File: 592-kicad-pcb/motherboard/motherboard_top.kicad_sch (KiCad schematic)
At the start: 27 parts, among them J17 Conn_02x01, J18 Conn_02x01, J21 Conn_02x01, J22 Conn_02x01, J25 Conn_02x01, J26 Conn_02x01, U14 74CBTLV3257PW,118, U15 74CBTLV3257PW,118, U17 74CBTLV3257PW,118, U18 SN74LVC1G00DCK, U19 SN74LVC1G14DBV, U20 74CBTLV3257PW,118, U21 SN74LVC1G14DBV

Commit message: john's notes
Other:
- sheet pmic_on_boarding ports: added 5V0_EXTERNAL, 5V0_NUCLEO, 5V0_ON_BOARD, GND; removed none
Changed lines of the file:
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@@
 		(exclude_from_sim no)
 		(at 156.21 238.76 0)
-		(size 62.23 29.21)
+		(size 62.23 124.46)
 		(margins 0.9525 0.9525 0.9525 0.9525)
 		(stroke
@@
 	)
 	(sheet
-		(at 342.9 203.2)
+		(at 163.83 344.17)
 		(size 44.45 40.64)
 		(exclude_from_sim no)
@@
 		)
 		(property "Sheetname" "pmic_switching"
-			(at 342.9 202.4884 0)
+			(at 163.83 343.4584 0)
 			(effects
 				(font
@@
 		)
 		(property "Sheetfile" "pmic_switching.kicad_sch"
-			(at 342.9 244.4246 0)
+			(at 163.83 385.3946 0)
 			(effects
 				(font
@@
 	)
 	(sheet
-		(at 290.83 203.2)
+		(at 165.1 297.18)
 		(size 41.91 40.64)
 		(exclude_from_sim no)
@@
 		)
 		(property "Sheetname" "pmic_supplies"
-			(at 290.83 202.4884 0)
+			(at 165.1 296.4684 0)
 			(effects
 				(font
@@
 		)
 		(property "Sheetfile" "pmic_supplies.kicad_sch"
-			(at 290.83 244.4246 0)
+			(at 165.1 338.4046 0)
 			(effects
 				(font
@@
 	)
 	(sheet
-		(at 233.68 203.2)
+		(at 165.1 250.19)
 		(size 41.91 40.64)
 		(exclude_from_sim no)
@@
 		)
 		(property "Sheetname" "pmic_on_boarding"
-			(at 233.68 202.4884 0)
+			(at 165.1 249.4784 0)
 			(effects
 				(font
@@
 		)
 		(property "Sheetfile" "pmic_on_boarding.kicad_sch"
-			(at 233.68 244.4246 0)
+			(at 165.1 291.4146 0)
 			(effects
 				(font
@@
 			)
 		)
+		(pin "5V0_ON_BOARD" output
+			(at 165.1 259.08 180)
+			(effects
+				(font
+					(size 1.27 1.27)
+				)
+				(justify left)
+			)
+		)
+		(pin "5V0_NUCLEO" input
+			(at 165.1 264.16 180)
+			(effects
+				(font
+					(size 1.27 1.27)
+				)
+				(justify left)
+			)
+		)
+		(pin "GND" bidirectional
+			(at 185.42 290.83 270)
+			(effects
+				(font
+					(size 1.27 1.27)
+				)
+				(justify left)
+			)
+		)
+		(pin "5V0_EXTERNAL" input
+			(at 207.01 261.62 0)
+			(effects
+				(font
+					(size 1.27 1.27)
+				)
+				(justify right)
+			)
+		)

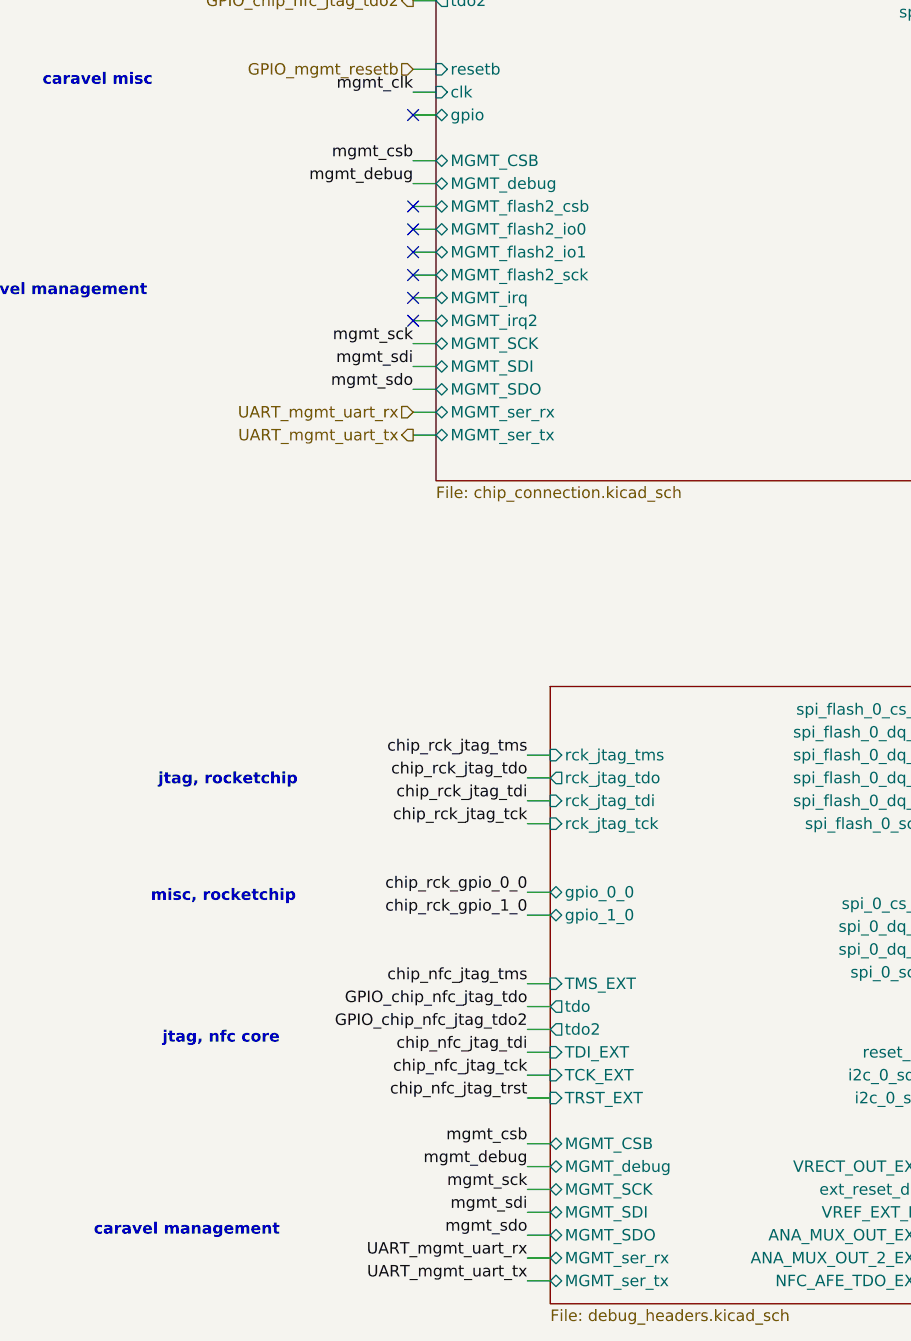
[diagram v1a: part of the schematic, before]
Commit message: map to STM pins
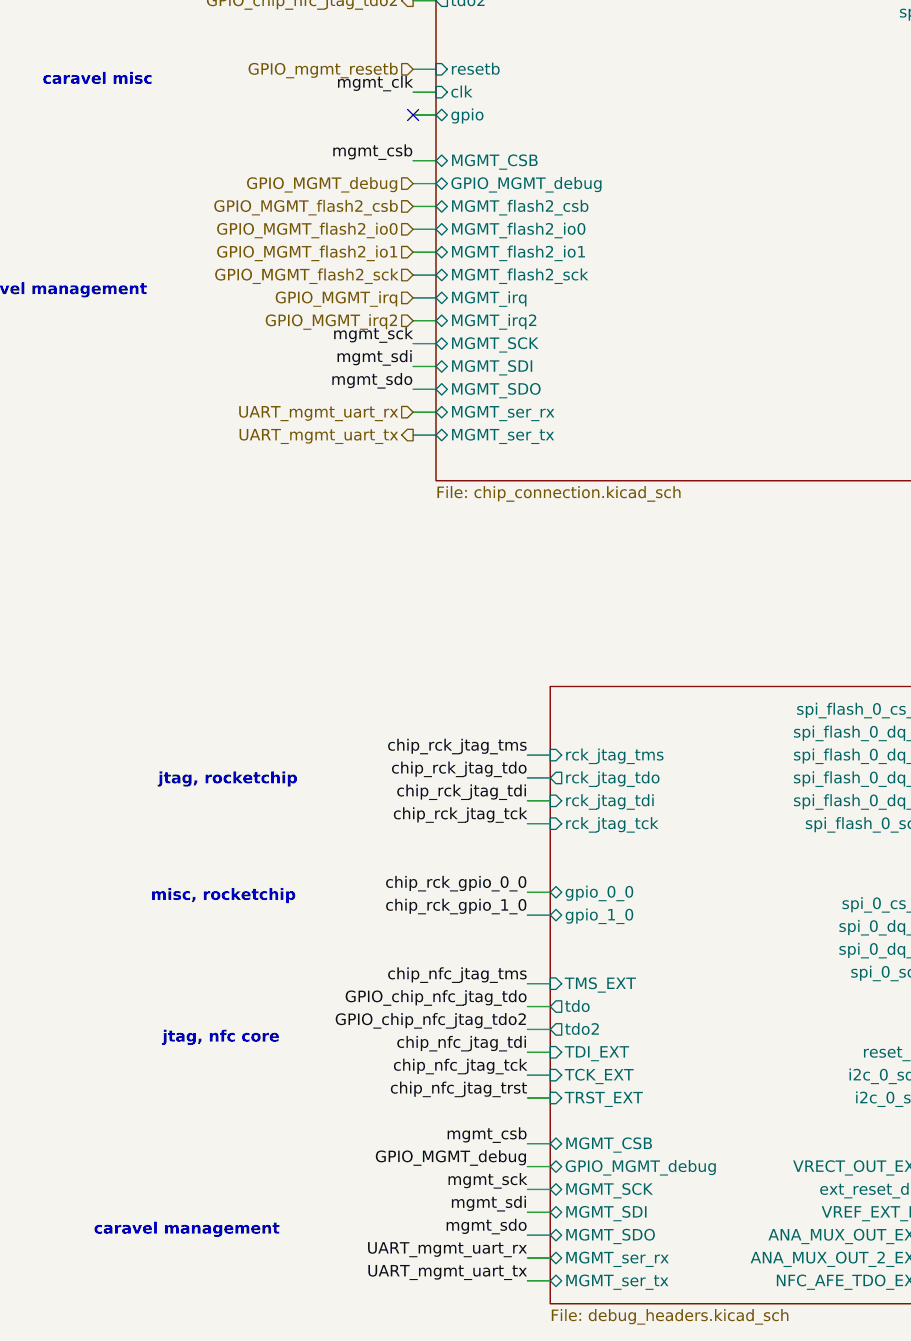
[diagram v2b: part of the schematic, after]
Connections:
- no-connect marks 14 -> 8
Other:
- sheet chip_connection ports: added GPIO_MGMT_debug; removed MGMT_debug
- sheet debug_headers ports: added GPIO_MGMT_debug; removed MGMT_debug
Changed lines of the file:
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@@
 	)
 	(no_connect
-		(at 80.01 115.57)
-	)
-	(no_connect
-		(at 80.01 105.41)
-	)
-	(no_connect
-		(at 80.01 113.03)
-	)
-	(no_connect
 		(at 166.37 246.38)
 	)
@@
 	)
 	(no_connect
-		(at 80.01 107.95)
-	)
-	(no_connect
-		(at 80.01 110.49)
-	)
-	(no_connect
 		(at 405.13 152.4)
 	)
@@
 	)
 	(no_connect
-		(at 80.01 102.87)
-	)
-	(no_connect
 		(at 389.89 149.86)
 	)
@@
 		)
 	)
-	(label "mgmt_debug"
+	(label "GPIO_MGMT_debug"
 		(at 92.71 209.55 180)
 		(effects
@@
 		)
 	)
-	(label "mgmt_debug"
-		(at 80.01 100.33 180)
-		(effects
-			(font
-				(size 1.27 1.27)
-			)
-			(justify right bottom)
-		)
-	)
 	(label "rck_mem_source_enB"
 		(at 364.49 66.04 270)
@@
 		)
 	)
+	(hierarchical_label "GPIO_MGMT_debug"
+		(shape input)
+		(at 80.01 100.33 180)
+		(effects
+			(font
+				(size 1.27 1.27)
+			)
+			(justify right)
+		)
+	)
 	(hierarchical_label "GPIO_ftdi_jtag_src_en"
 		(shape input)
@@
 		)
 	)
+	(hierarchical_label "GPIO_MGMT_flash2_io1"
+		(shape input)
+		(at 80.01 107.95 180)
+		(effects
+			(font
+				(size 1.27 1.27)
+			)
+			(justify right)
+		)
+	)
+	(hierarchical_label "GPIO_MGMT_flash2_csb"
+		(shape input)
+		(at 80.01 102.87 180)
+		(effects
+			(font
+				(size 1.27 1.27)
+			)
+			(justify right)
+		)
+	)
+	(hierarchical_label "GPIO_MGMT_flash2_io0"
+		(shape input)
+		(at 80.01 105.41 180)
+		(effects
+			(font
+				(size 1.27 1.27)
+			)
+			(justify right)
+		)
+	)
+	(hierarchical_label "GPIO_MGMT_flash2_sck"
+		(shape input)
+		(at 80.01 110.49 180)
+		(effects
+			(font
+				(size 1.27 1.27)
+			)
+			(justify right)
+		)
+	)
+	(hierarchical_label "GPIO_MGMT_irq"
+		(shape input)
+		(at 80.01 113.03 180)
+		(effects
+			(font
+				(size 1.27 1.27)
+			)
+			(justify right)
+		)
+	)
+	(hierarchical_label "GPIO_MGMT_irq2"
+		(shape input)
+		(at 80.01 115.57 180)
+		(effects
+			(font
+				(size 1.27 1.27)
+			)
+			(justify right)
+		)
+	)
 	(hierarchical_label "GPIO_rck_mem_sel_sdB"
 		(shape input)
@@
 			)
 		)
-		(pin "MGMT_debug" bidirectional
+		(pin "GPIO_MGMT_debug" bidirectional
 			(at 95.25 209.55 180)
 			(effects
@@
 			)
 		)
-		(pin "MGMT_debug" bidirectional
+		(pin "GPIO_MGMT_debug" bidirectional
 			(at 82.55 100.33 180)
 			(effects

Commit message: updates to routing
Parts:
- renumbered C38 to C37, C41 to C38, C34 to C39, C35 to C41, J26 to J23, J17 to J24, J18 to J26, R56 to R52, R57 to R53, R49 to R54, R48 to R55, R50 to R56, R52 to R57, R53 to R58, U19 to U15, U18 to U16, U14 to U17, U21 to U18, U17 to U19, U15 to U20, U20 to U21
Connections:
- net GPIO_chip_nfc_jtag_tdo: now also U19.3; no longer U19.10
- net chip_nfc_jtag_tms: now also U19.10; no longer U19.3
- net chip_rck_jtag_tdo: now also U19.2; no longer U19.11
- net chip_rck_jtag_tms: now also U19.11; no longer U19.2
- net ftdi1_jtag_tdo: now also U19.4; no longer U19.9
- net ftdi1_jtag_tms: now also U19.9; no longer U19.4

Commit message: finalize termination
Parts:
- added C53: 10n, symbol Device:C_Small
- added R10, R14, R15, R16, R19, R71, R72, R8, R9, R98, R99: 10k, Resistor_SMD:R_0402_1005Metric, symbol Device:R_Small
- added R104, R17: 1M, Resistor_SMD:R_0402_1005Metric, symbol Device:R_Small
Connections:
- net +3V3: now also R10.1, R14.1, R15.1, R16.1, R71.1, R72.1, R8.1, R9.1, R98.1, R99.1
- net GND: now also C53.2, R104.2, R17.2, R19.2
- net chip_nfc_jtag_tck: now also R17.1
- net chip_nfc_jtag_tdi: now also R14.2
- net chip_nfc_jtag_tms: now also R16.2, R9.2
- net chip_nfc_jtag_trst: now also C53.1, R19.1
- net chip_rck_jtag_tck: now also R104.1
- net chip_rck_jtag_tdi: now also R10.2
- net chip_rck_jtag_tms: now also R15.2, R8.2
- net ftdi_spi_cs: now also R71.2
- net ftdi_spi_sck: now also R72.2
- net rck_mem_cs: now also R98.2
- net rck_mem_sck: now also R99.2
- net GPIO_SPI_MGMT_enable renamed GPIO_MGMT_enable
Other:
- sheet chip_connection ports: added GPIO_MGMT_enable; removed none
- note added: "SPI pull-ups to ensure OK state w/out daughter"
- note added: "also allow disabling for off-chip mem"

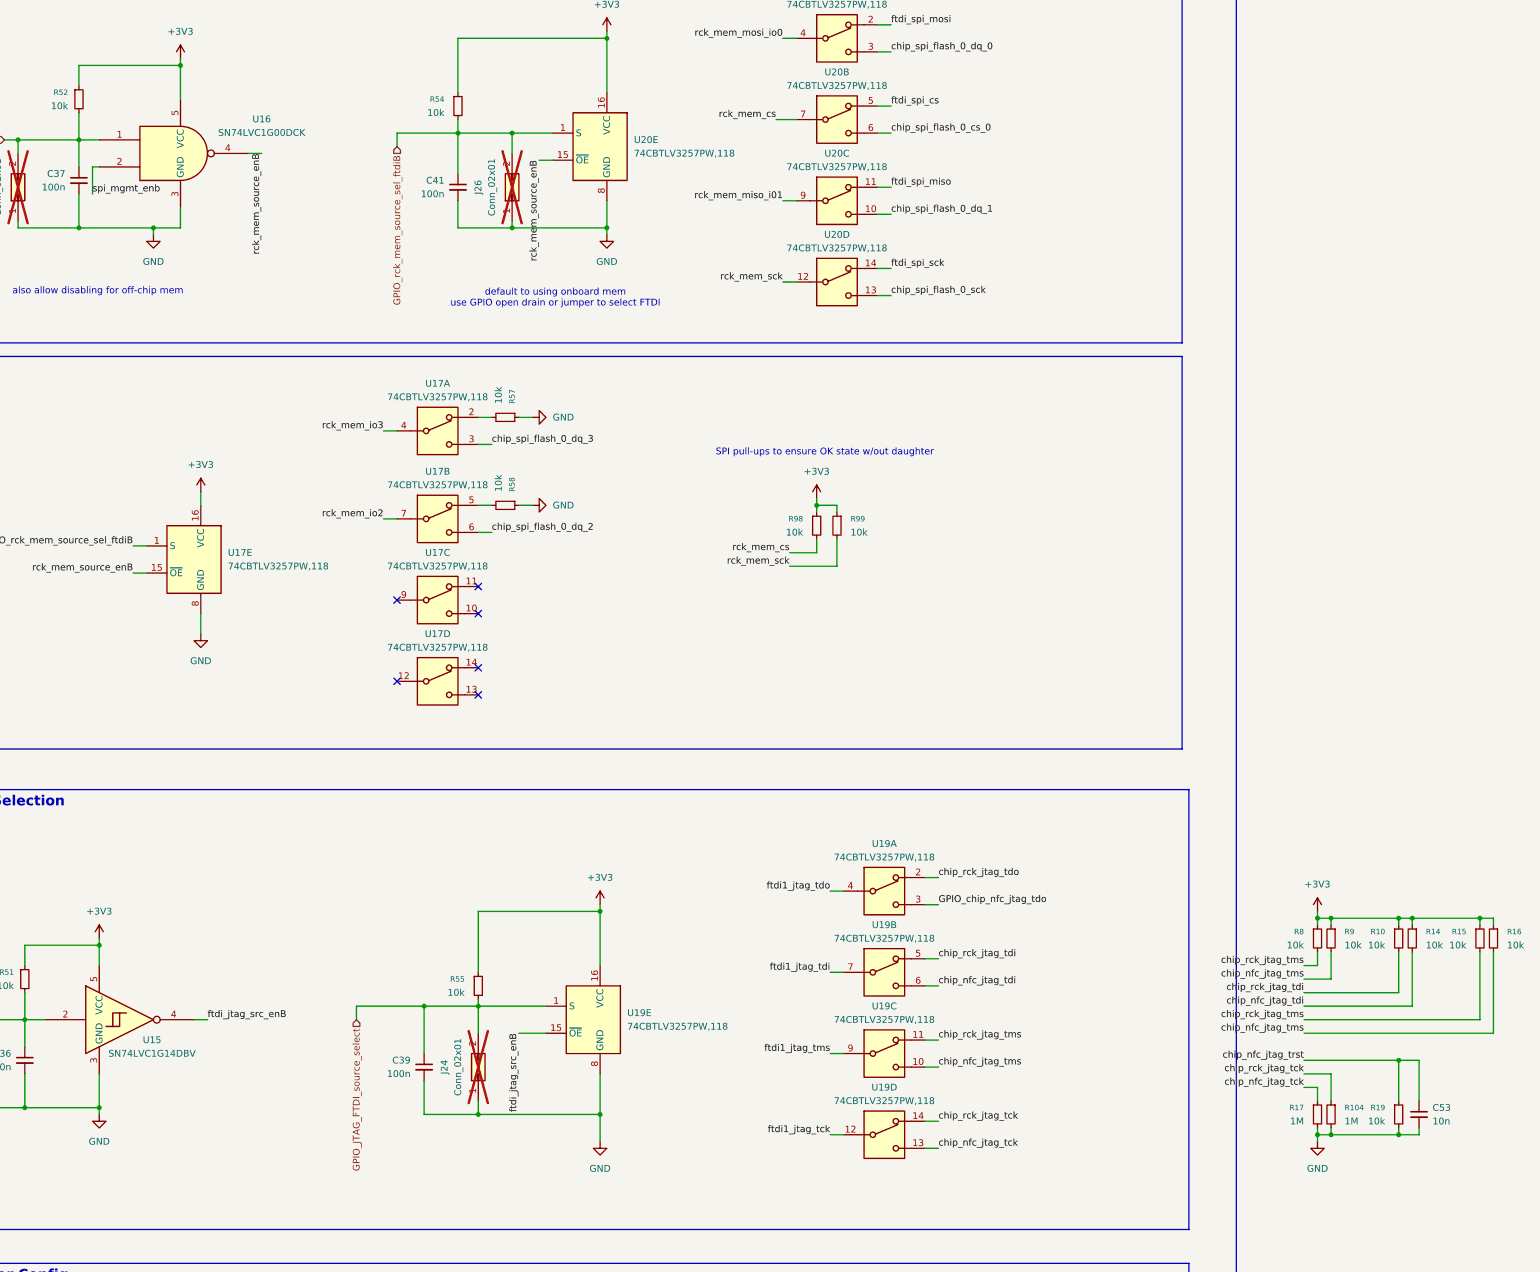
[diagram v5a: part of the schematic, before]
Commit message: update jlcpcb part numbers
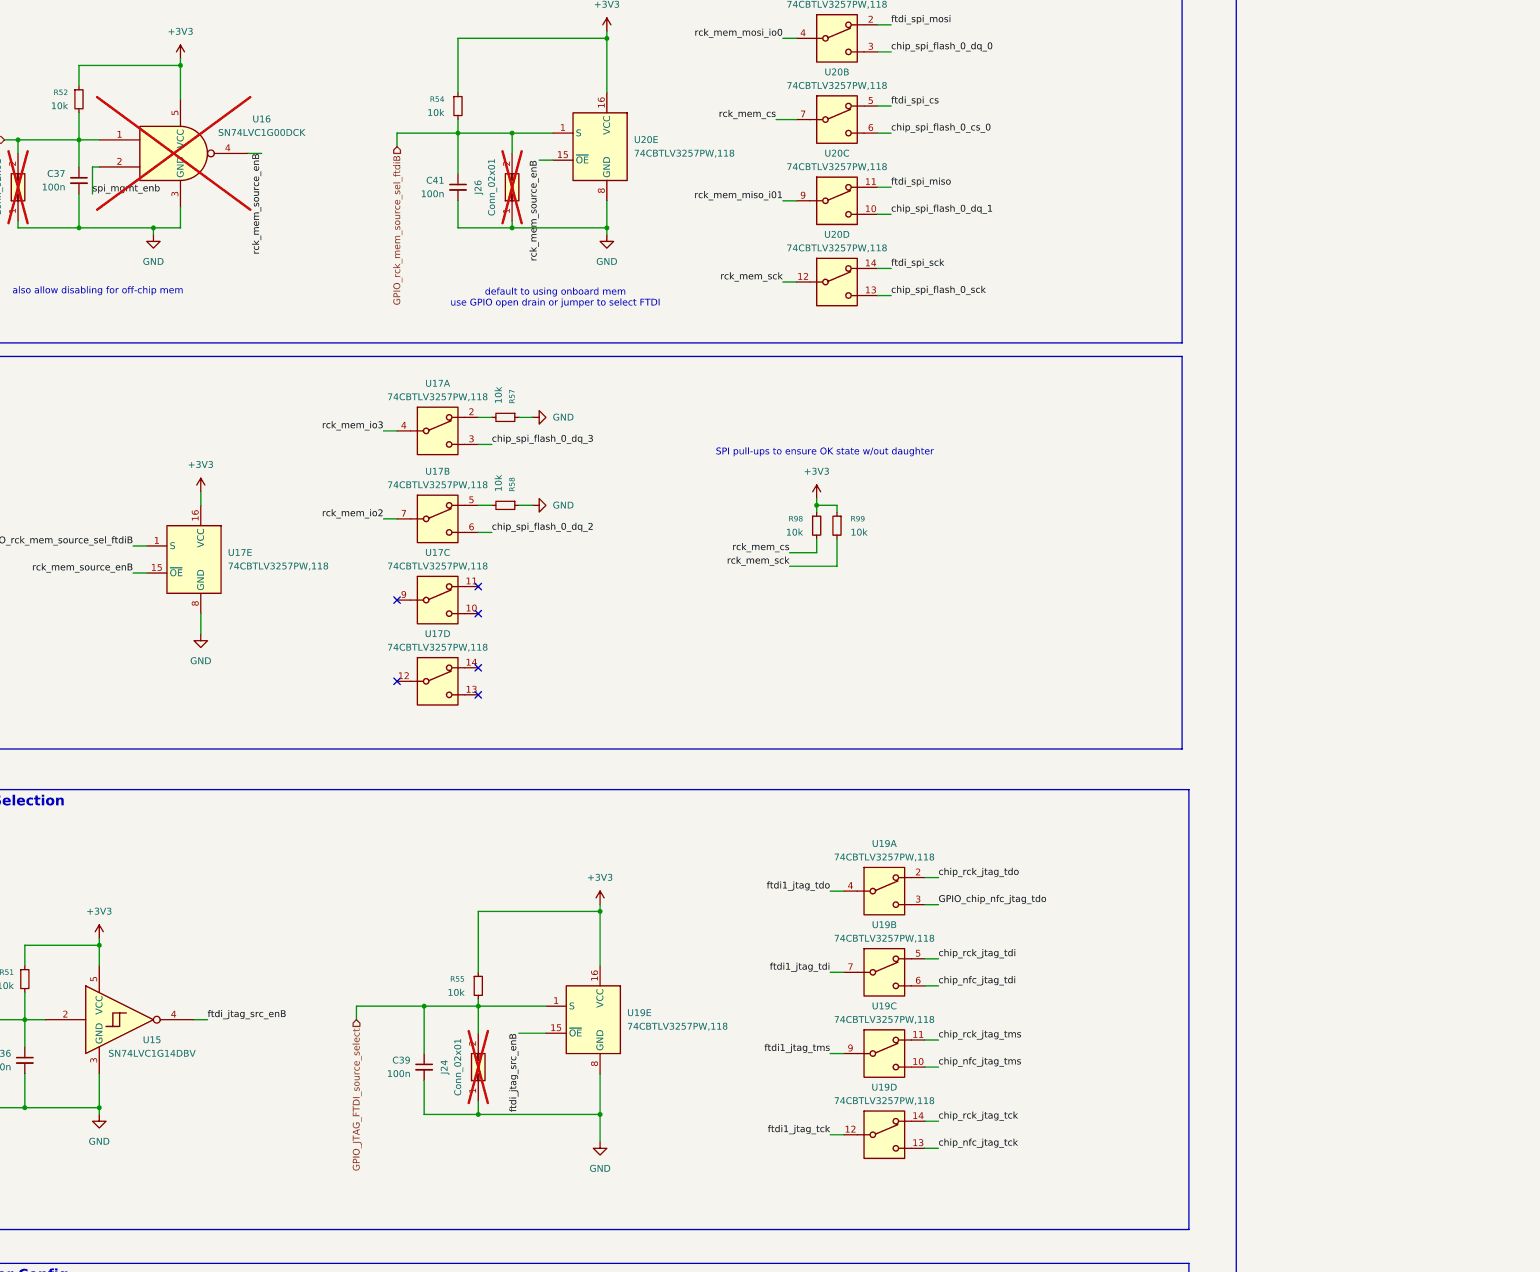
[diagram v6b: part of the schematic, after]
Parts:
- removed C53: 10n, symbol Device:C_Small
- removed R10, R14, R15, R16, R19, R8, R9: 10k, Resistor_SMD:R_0402_1005Metric, symbol Device:R_Small
- removed R104, R17: 1M, Resistor_SMD:R_0402_1005Metric, symbol Device:R_Small
- U16: now not fitted
